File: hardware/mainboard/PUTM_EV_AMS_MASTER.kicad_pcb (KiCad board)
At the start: 4 copper layers, 60 x 100 mm, 169 parts, among them IC3 BQ79600PWRQ1, IC6 AMC3330DWER, IC7 AMC3330DWER, IC8 ADC 24bit, IC9 LTC1799, J1 Conn_02x10_Odd_Even, J10 M300-MV10345M1, J2 XIAO ESP32S3 Sense, J3 Conn_02x04_Odd_Even, J4 FTSH-107-01-L-D-K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

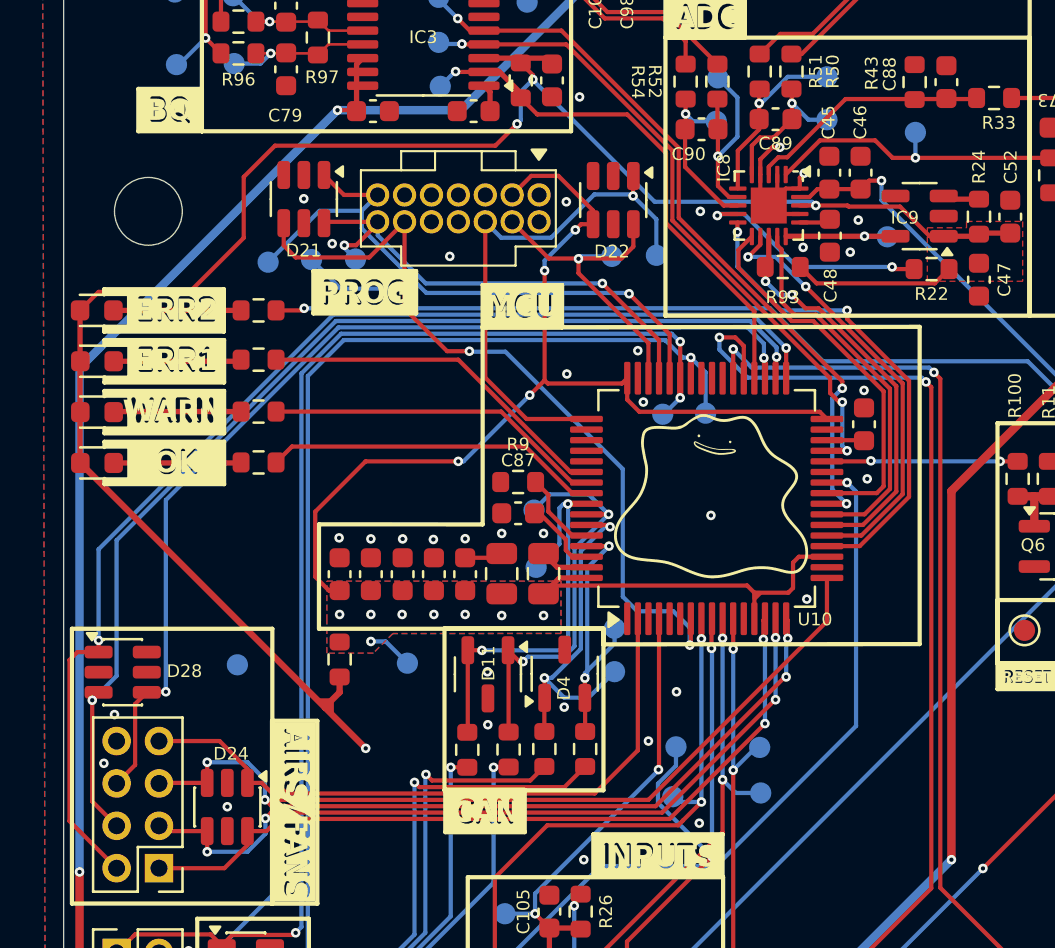
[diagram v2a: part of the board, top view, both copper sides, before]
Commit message: Fixed MCU Caps
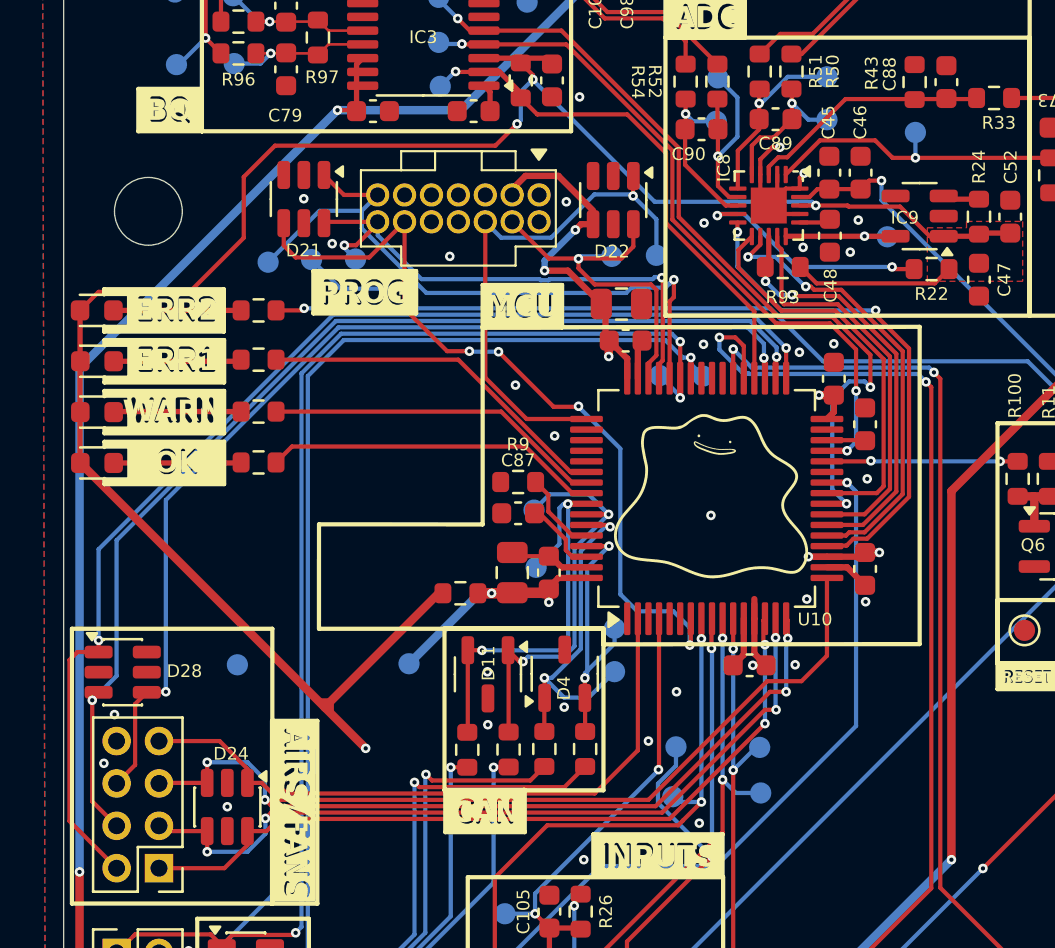
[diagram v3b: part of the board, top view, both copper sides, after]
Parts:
- moved C29 25.1 mm to (138.3, 94.4)
- moved C28 20.4 mm to (139.8, 103.4), turned to -90 degrees
- moved C25 15.2 mm to (128.5, 92.6), turned to 0 degrees
- moved C24 14.1 mm to (134.4, 107.9), turned to 180 degrees
- moved C36 13.9 mm to (128.3, 90.9), turned to 0 degrees
- moved C23 8.40 mm to (124.9, 103.5)
- moved R3 6.50 mm to (120.7, 104.5), turned to 0 degrees
- moved TX1 1.83 mm to (130.1, 94.2)
- moved RX1 1.75 mm to (132.2, 94.3)
- moved C70 1.48 mm to (123.2, 103.5)
- moved TP3 0.08 mm to (118.3, 107.8)
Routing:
- net +3.3VMCU: track 67.7 -> 42.4 mm, vias 12 -> 9
- net GND: track 13.6 -> 19.7 mm, vias 42 -> 38
- net +3.3VIO: track 149.0 -> 155.1 mm
- net /UCRX: track 35.7 -> 39.3 mm
- net /UART_DBG_RX: track 28.9 -> 31.2 mm
- net /UART_DBG_TX: track 23.3 -> 25.4 mm
- net /SWDIO: track 17.1 -> 19.0 mm
- net /UART_RX: track 61.9 -> 60.1 mm
- net /UCTX: track 31.7 -> 33.5 mm
- net /FAN4-: track 38.6 -> 39.6 mm
- net /ADC_MOSI: track 18.2 -> 19.1 mm
- net /ADC_SCK: track 20.6 -> 21.5 mm
- net /~{ADC_DRY}: track 18.3 -> 19.2 mm
- net /ADC_MISO: track 18.9 -> 19.8 mm
- net /~{CS_MISO}: track 23.0 -> 23.8 mm
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- added copper zone on In2.Cu, net +3.3VMCU
- removed copper zone on B.Cu, net +3.3VMCU
- removed copper zone on F.Cu, net +3.3VMCU

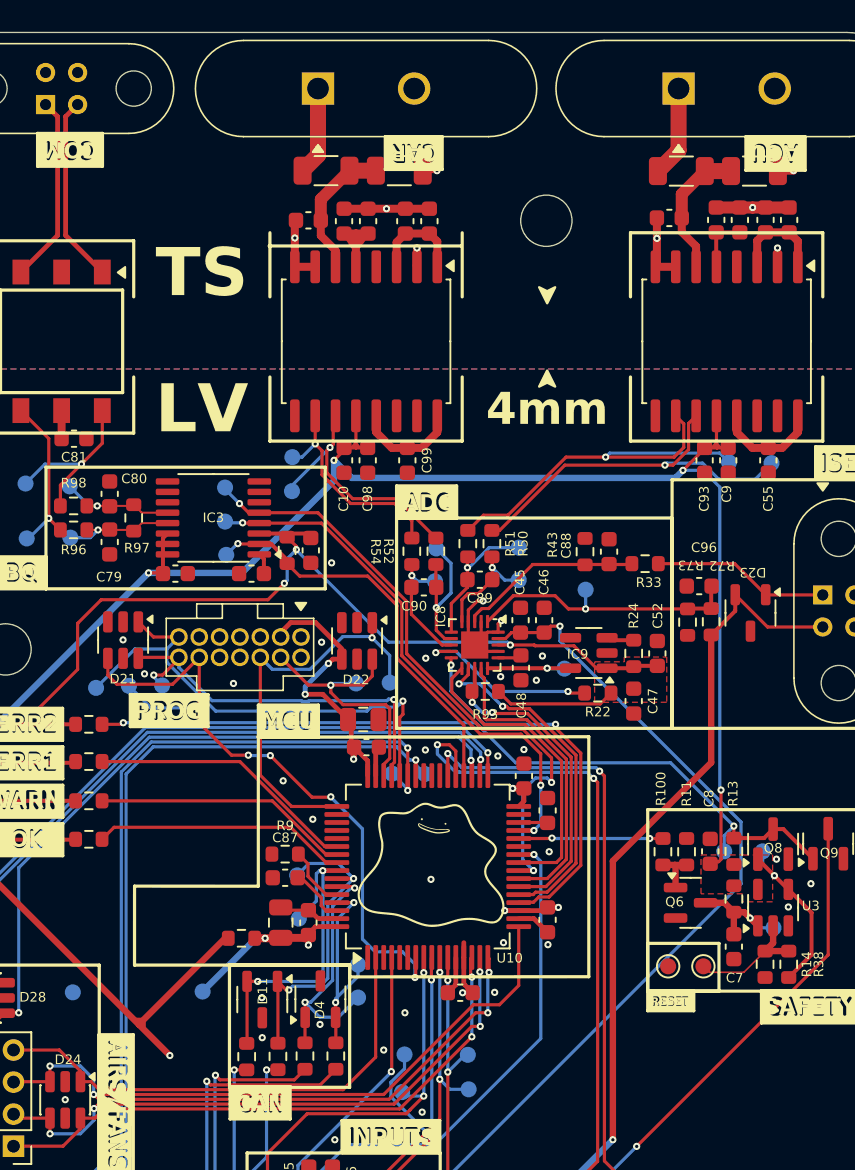
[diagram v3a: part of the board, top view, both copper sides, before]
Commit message: Better silkscreen placement and routing
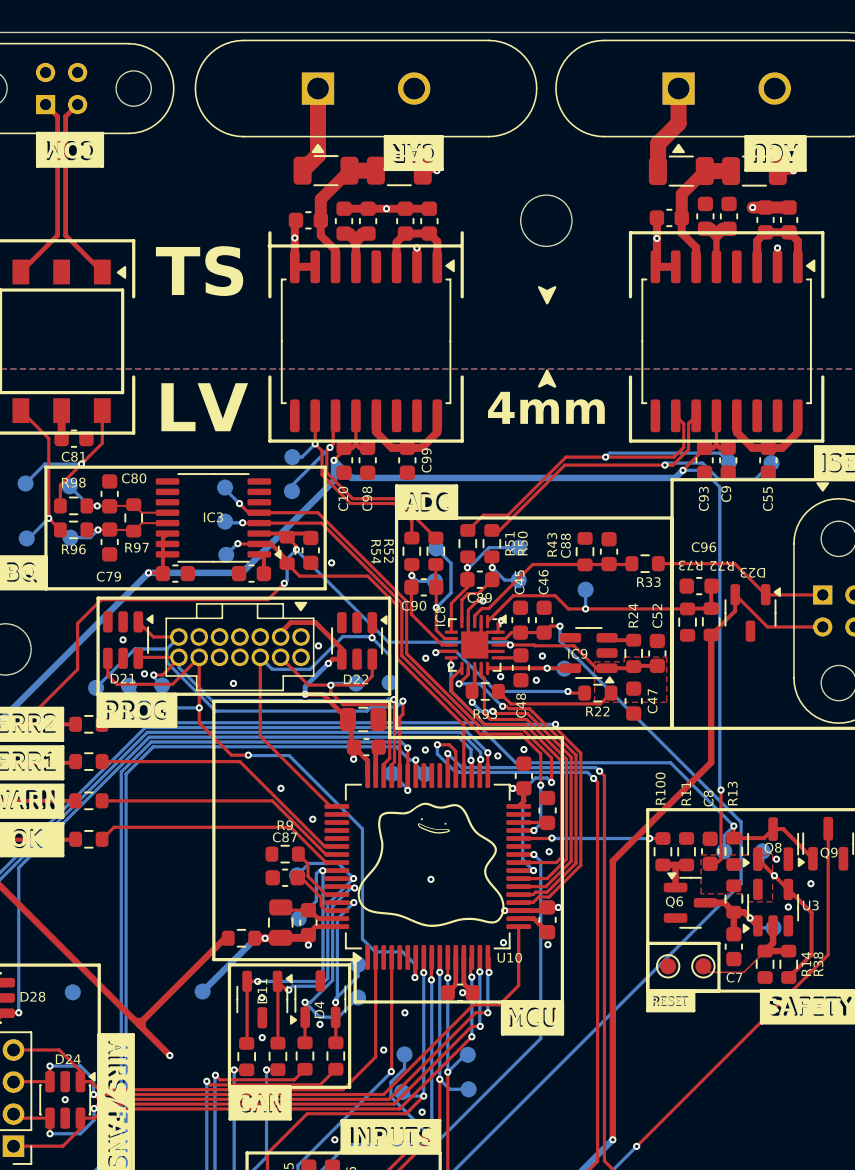
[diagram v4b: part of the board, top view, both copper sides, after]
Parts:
- moved C54 0.71 mm to (151.2, 59.5)
- moved C94 0.71 mm to (149.7, 59.5)
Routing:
- net /IsolationBarrier/ACU_GND: track 11.1 -> 8.82 mm
- net /SWCLK: track 25.3 -> 23.9 mm
- net +3.3VMCU: track 42.4 -> 41.4 mm
- net /IsolationBarrier/ACU_LDO: track 3.63 -> 4.15 mm
- net /NRST: track 42.7 -> 42.6 mm, vias 5 -> 3
- net GND: vias 38 -> 37
